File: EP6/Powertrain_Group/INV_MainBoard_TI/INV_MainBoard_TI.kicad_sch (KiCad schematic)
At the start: 33 parts, among them J1 FX26-30P-1SV, J10 CAN, J11 CAN, J12 CAN, J2 motorSense, J7 phase control monitor, J8 current, J9 CAN, Q1 2N7002, Q2 2N7002

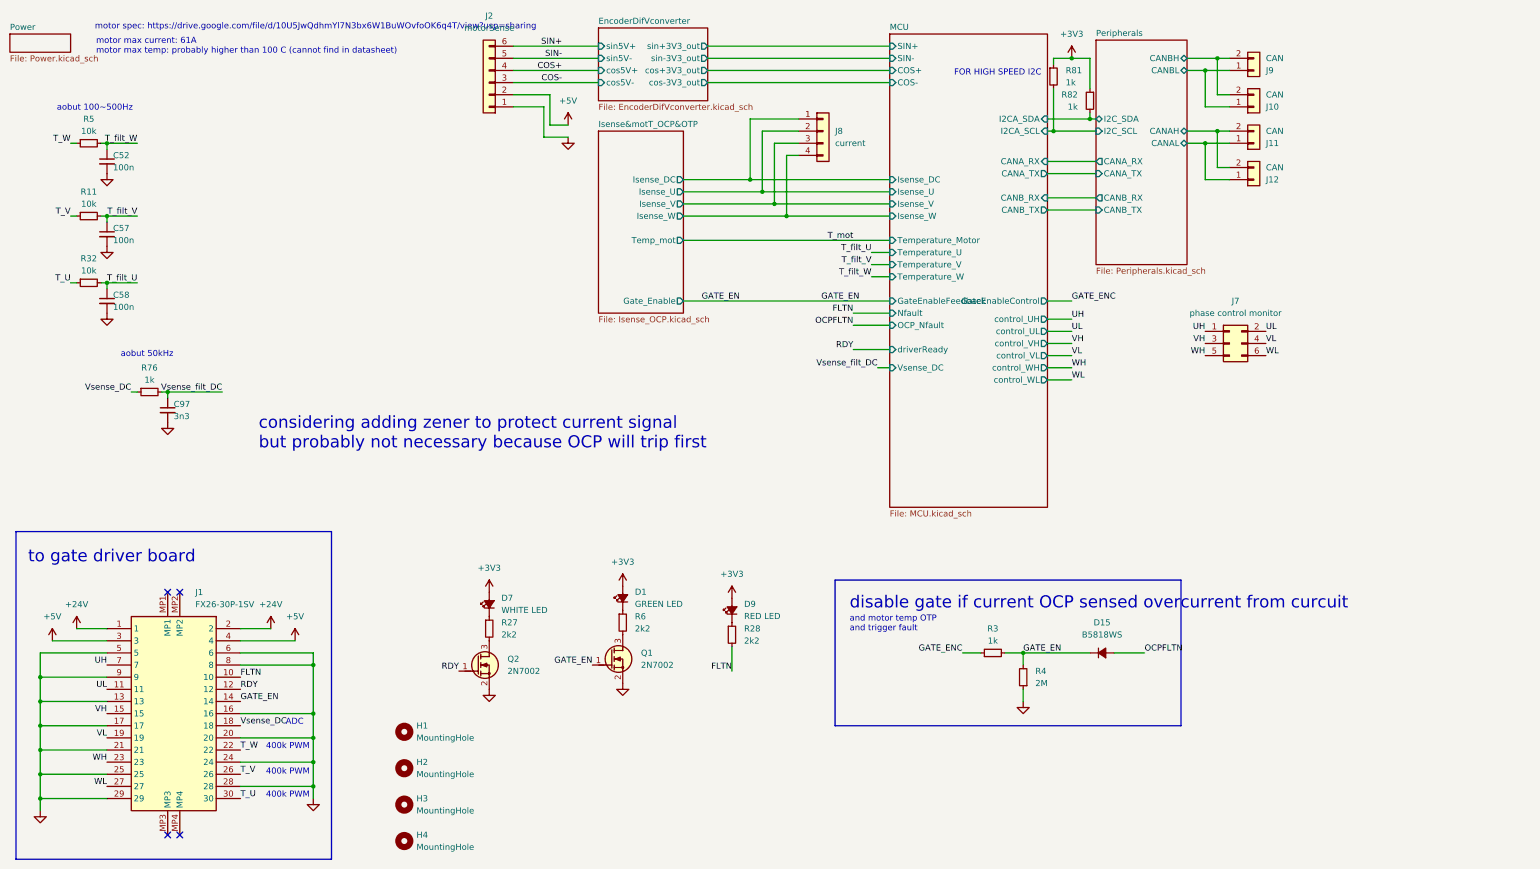
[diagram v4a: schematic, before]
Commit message: add comments to INV boards after testing JLC PCBs
INV boards included:
INV_GateDriver: mainly about QSPI SPRAM
INV_MainBoard_STM32: mainly about mistake VINC of LM26420
INV_MainBoard_TI: mainly about trace too long and incorrect spec of Rg
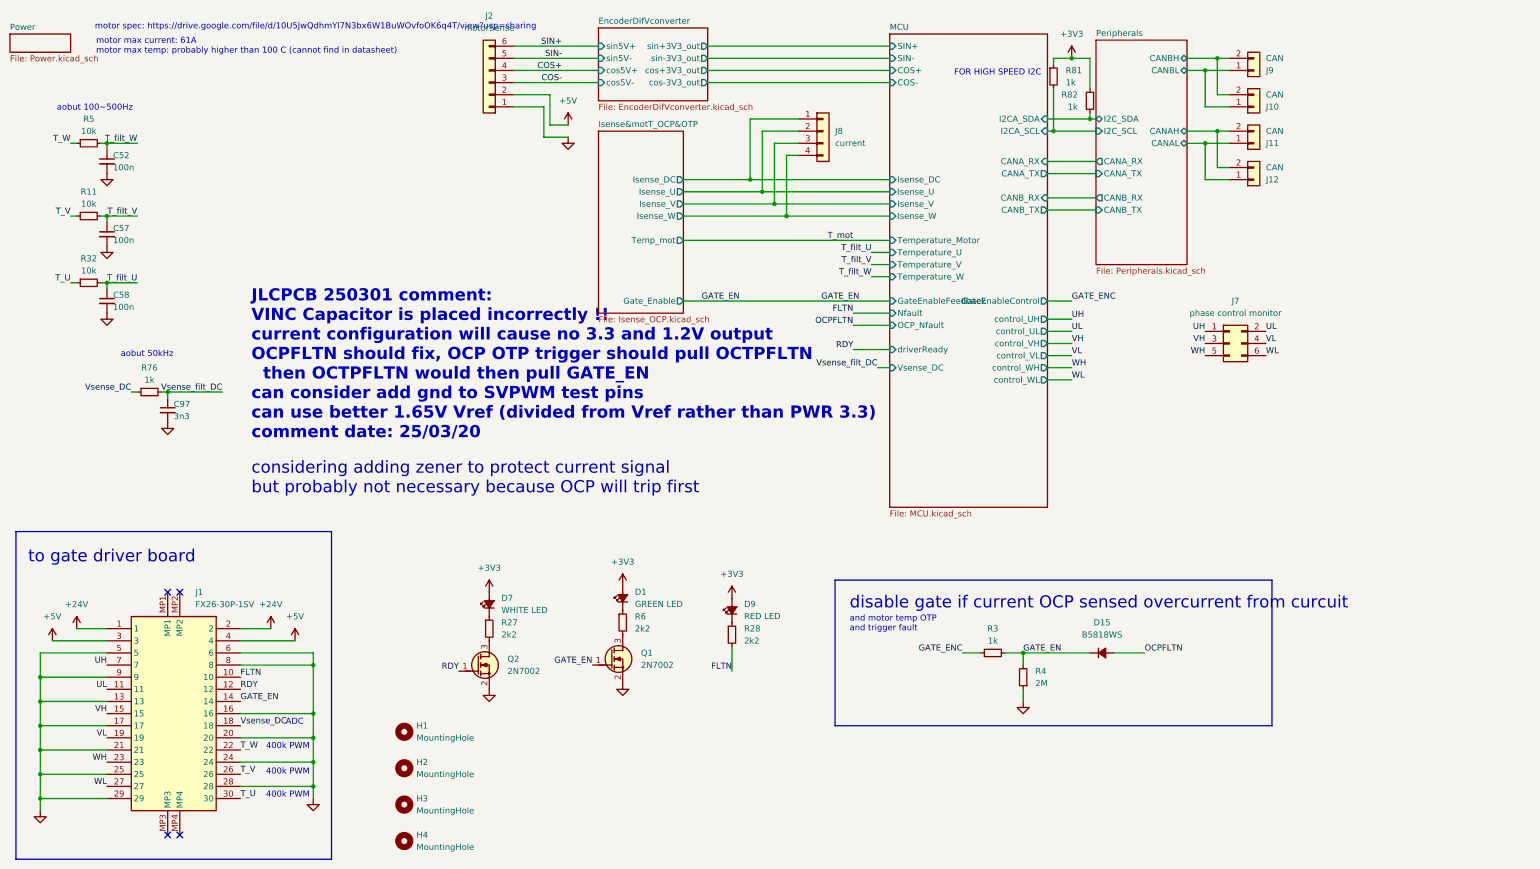
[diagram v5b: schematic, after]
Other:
- note added: "JLCPCB 250301 comment: VINC Capacitor is placed incorrectly !! current configuration will cause no 3.3 and 1.2V output OCPFLTN should fix, OCP OTP trigger should pull OCTPFLTN then OCTPFLTN would then pull GATE_EN can consider add gnd to SVPWM test pins can use better 1.65V Vref (divided from Vref rather than PWR 3.3) comment date: 25/03/20"
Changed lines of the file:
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@@
 	(rectangle
 		(start 187.96 132.08)
-		(end 260.35 162.56)
+		(end 279.4 162.56)
 		(stroke
 			(width 0)
@@
 		)
 	)
+	(text "JLCPCB 250301 comment:\nVINC Capacitor is placed incorrectly !!\ncurrent configuration will cause no 3.3 and 1.2V output\nOCPFLTN should fix, OCP OTP trigger should pull OCTPFLTN\n  then OCTPFLTN would then pull GATE_EN\ncan consider add gnd to SVPWM test pins\ncan use better 1.65V Vref (divided from Vref rather than PWR 3.3)\ncomment date: 25/03/20"
+		(exclude_from_sim no)
+		(at 65.786 71.12 0)
+		(effects
+			(font
+				(size 2.54 2.54)
+				(thickness 0.508)
+				(bold yes)
+				(color 255 0 0 1)
+			)
+			(justify left top)
+		)
+	)
 	(text "disable gate if current OCP sensed overcurrent from curcuit"
 		(exclude_from_sim no)
@@
 	(text "considering adding zener to protect current signal\nbut probably not necessary because OCP will trip first"
 		(exclude_from_sim no)
-		(at 67.31 97.79 0)
+		(at 65.786 107.188 0)
 		(effects
 			(font

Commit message: update INV_MainBoard_TI to V2.0
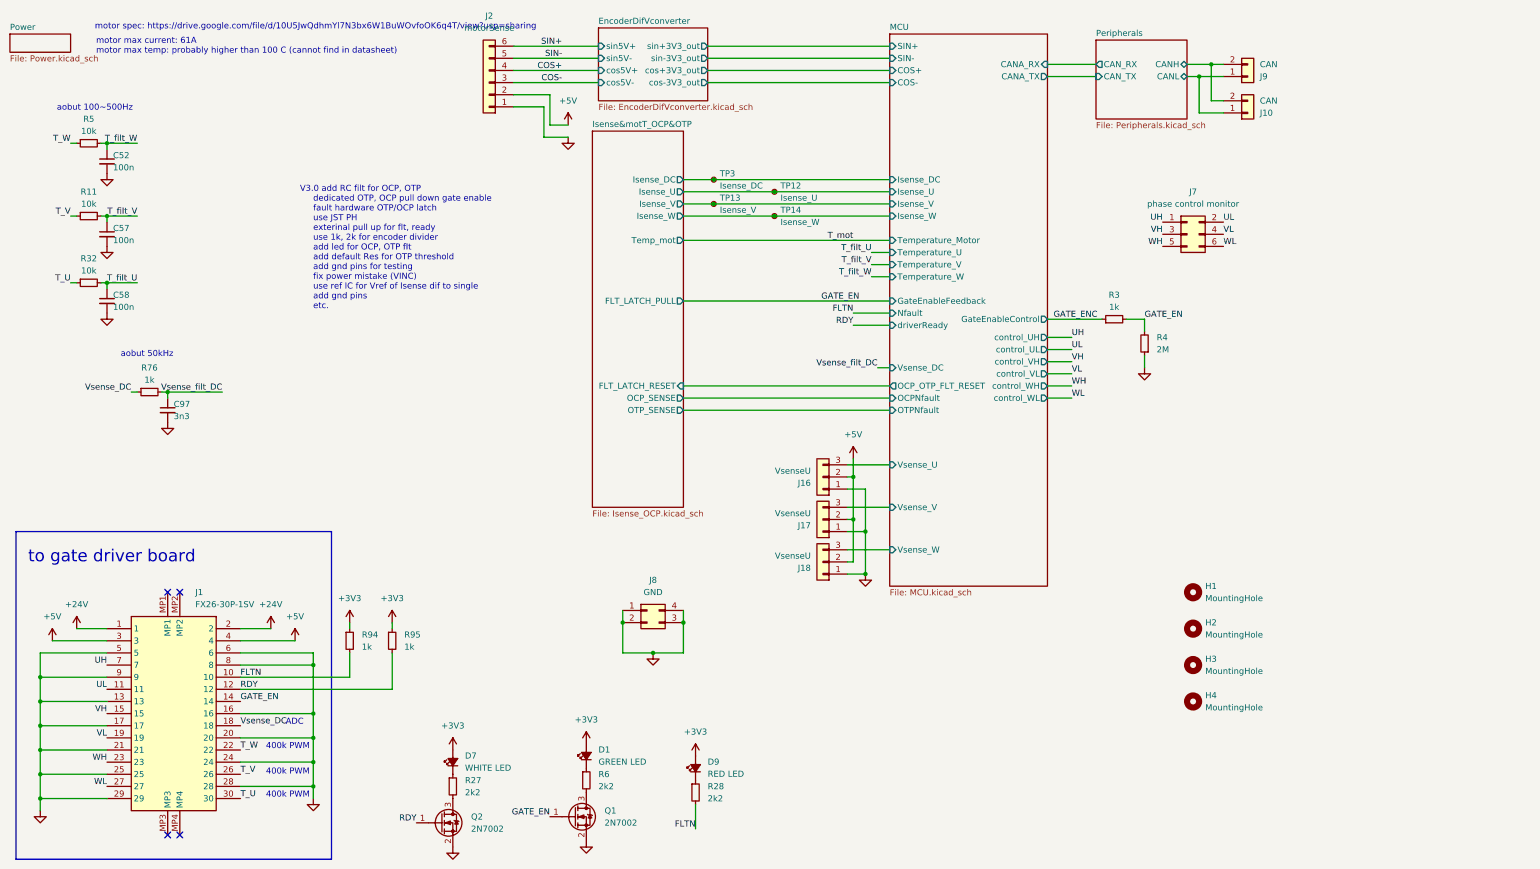
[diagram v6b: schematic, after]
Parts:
- removed D15: B5818WS, Diode_SMD:D_SOD-323, symbol Device:D_Small_Filled
- removed J11, J12: CAN, Connector_JST:JST_XH_B2B-XH-A_1x02_P2.50mm_Vertical, symbol Connector_Generic:Conn_01x02
- removed J8: current, Connector_PinHeader_2.54mm:PinHeader_1x04_P2.54mm_Vertical, symbol Connector_Generic:Conn_01x04
- removed Q1, Q2: 2N7002, PCM_Package_TO_SOT_SMD_AKL:SOT-23, symbol PCM_Transistor_MOSFET_AKL:2N7002
- removed R81, R82: 1k, Resistor_SMD:R_0402_1005Metric, symbol Device:R_Small
- added J16, J17, J18: VsenseU, Connector_PinSocket_2.00mm:PinSocket_1x03_P2.00mm_Vertical, symbol Connector_Generic:Conn_01x03
- added J8: GND, Connector_PinHeader_2.54mm:PinHeader_2x02_P2.54mm_Vertical, symbol Connector_Generic:Conn_02x02_Counter_Clockwise
- added Q1, Q2: 2N7002, Package_TO_SOT_SMD:SOT-23, symbol Transistor_FET:2N7002
- added R94, R95: 1k, Resistor_SMD:R_0402_1005Metric, symbol Device:R_Small
- added TP12: Isense_U, TestPoint:TestPoint_Pad_D1.0mm, symbol Connector:TestPoint_Small
- added TP13: Isense_V, TestPoint:TestPoint_Pad_D1.0mm, symbol Connector:TestPoint_Small
- added TP14: Isense_W, TestPoint:TestPoint_Pad_D1.0mm, symbol Connector:TestPoint_Small
- added TP3: Isense_DC, TestPoint:TestPoint_Pad_D1.0mm, symbol Connector:TestPoint_Small
- J1: footprint FX2630P1SV -> SamacSys_Parts_EP6:FX2630P1SV
- J2: footprint Connector_JST:JST_XH_B6B-XH-A_1x06_P2.50mm_Vertical -> Connector_JST:JST_PH_B6B-PH-K_1x06_P2.00mm_Vertical
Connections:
- net +3V3: now also R94.1, R95.1
- net +5V: now also J16.2 (Pin_2), J17.2 (Pin_2), J18.2 (Pin_2)
- net FLTN: now also R94.2
- net GATE_EN: now also Q1.1 (G)
- net GND: now also J16.1 (Pin_1), J17.1 (Pin_1), J18.1 (Pin_1), J8.1 (Pin_1), J8.2 (Pin_2), J8.3 (Pin_3), J8.4 (Pin_4), Q1.2 (S), Q2.2 (S)
- net Isense&motT_OCP&OTP/Isense_DC: now also TP3.1
- net Isense&motT_OCP&OTP/Isense_U: now also TP12.1
- net Isense&motT_OCP&OTP/Isense_V: now also TP13.1
- net Isense&motT_OCP&OTP/Isense_W: now also TP14.1
- net RDY: now also Q2.1 (G), R95.2
- net at R27.2: now also Q2.3 (D)
- net at R6.2: now also Q1.3 (D)
- net Peripherals/CANBH renamed Peripherals/CANH
- net Peripherals/CANBL renamed Peripherals/CANL
- new net MCU/Vsense_U: J16.3 (Pin_3)
- new net MCU/Vsense_V: J17.3 (Pin_3)
- new net MCU/Vsense_W: J18.3 (Pin_3)
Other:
- sheet Isense&motT_OCP&OTP ports: added FLT_LATCH_PULL, FLT_LATCH_RESET, OCP_SENSE, OTP_SENSE; removed Gate_Enable
- sheet MCU ports: added OCPNfault, OCP_OTP_FLT_RESET, OTPNfault, Vsense_U, Vsense_V, Vsense_W; removed CANB_RX, CANB_TX, I2CA_SCL, I2CA_SDA, OCP_Nfault
- sheet Peripherals ports: added CANH, CANL, CAN_RX, CAN_TX; removed CANAH, CANAL, CANA_RX, CANA_TX, CANBH, CANBL, CANB_RX, CANB_TX, I2C_SCL, I2C_SDA
- note added: "V3.0 add RC filt for OCP, OTP dedicated OTP, OCP pull down gate enable fault hardware OTP/OCP latch use JST PH exterinal pull up for flt, ready use 1k, 2k for encoder divider add led for OCP, OTP flt add default Res for OTP threshold add gnd pins for testing fix power mistake (VINC) use ref IC for Vref of Isense dif to single add gnd pins etc."
- note removed: "FOR HIGH SPEED I2C"
- note removed: "JLCPCB 250301 comment: VINC Capacitor is placed incorrectly !! current configuration will cause no 3.3 and 1.2V output OCPFLTN should fix, OCP OTP trigger should pull OCTPFLTN then OCTPFLTN would then pull GATE_EN can consider add gnd to SVPWM test pins can use better 1.65V Vref (divided from Vref rather than PWR 3.3) comment date: 25/03/20"
- note removed: "and motor temp OTP"
- note removed: "and trigger fault"
- note removed: "considering adding zener to protect current signal but probably not necessary because OCP will trip first"
- note removed: "disable gate if current OCP sensed overcurrent from curcuit"
- moved on the sheet: D1, D7, D9, H1, H2, H3, H4, J10, J7, J9, R27, R28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
